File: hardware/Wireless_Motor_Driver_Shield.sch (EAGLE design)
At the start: 84 parts, among them Q1 MOSFET-NCHANNELBSS138, Q2 MOSFET-NCHANNELBSS138, U1 XBEE-1XBEE-1_LOCK, U2 ARDUINO, U3 TB6612FNG

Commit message: Updated after self Eng Design Rules Check
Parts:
- D1: value Red -> Yellow; device SparkFun-LED:LED-RED0603 -> SparkFun-LED:LED-YELLOW0603
- D3: value Yellow -> Red; device SparkFun-LED:LED-YELLOW0603 -> SparkFun-LED:LED-RED0603
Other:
- note added: "B. Huang Revised by Shawn Hymel"
- note added: "Connects Arduino A4 to SDA pin on R3 shield and SDA pin under XBEE radio."
- note removed: "B. Huang Modified by Shawn Hymel"
- moved on the sheet: SJ3, SJ4
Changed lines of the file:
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@@
 <setting verticaltext="up"/>
 </settings>
-<grid distance="0.1" unitdist="inch" unit="inch" style="lines" multiple="1" display="no" altdistance="0.01" altunitdist="inch" altunit="inch"/>
+<grid distance="0.1" unitdist="inch" unit="inch" style="lines" multiple="1" display="yes" altdistance="0.01" altunitdist="inch" altunit="inch"/>
 <layers>
 <layer number="1" name="Top" color="4" fill="1" visible="no" active="no"/>
@@
 <part name="LOGO4" library="SparkFun-Aesthetics" deviceset="SFE_LOGO_NAME_FLAME" device=".1_INCH" value="SFE_LOGO_NAME_FLAME.1_INCH"/>
 <part name="JP22" library="SparkFun-Connectors" deviceset="M04" device="LOCK"/>
-<part name="D1" library="SparkFun-LED" deviceset="LED-RED" device="0603" value="Red"/>
 <part name="D2" library="SparkFun-LED" deviceset="LED-GREEN" device="0603" value="Green"/>
 <part name="R6" library="SparkFun-Resistors" deviceset="1KOHM-1/10W-1%(0603)" device="" value="1K"/>
 <part name="R7" library="SparkFun-Resistors" deviceset="1KOHM-1/10W-1%(0603)" device="" value="1K"/>
-<part name="D3" library="SparkFun-LED" deviceset="LED-YELLOW" device="0603" value="Yellow"/>
 <part name="R8" library="SparkFun-Resistors" deviceset="1KOHM-1/10W-1%(0603)" device="" value="1K"/>
 <part name="GND5" library="SparkFun" deviceset="GND" device=""/>
@@
 <part name="F4" library="SparkFun-PowerIC" deviceset="PTC" device="SMD" value=""/>
 <part name="C3" library="SparkFun-Capacitors" deviceset="10UF" device="-1210-50V-20%" value="10uF"/>
+<part name="D3" library="SparkFun-LED" deviceset="LED-RED" device="0603" value="Red"/>
+<part name="D1" library="SparkFun-LED" deviceset="LED-YELLOW" device="0603" value="Yellow"/>
 </parts>
 <sheets>
@@
 <wire x1="259.08" y1="203.2" x2="259.08" y2="158.75" width="0.2032" layer="97" style="longdash"/>
 <text x="350.52" y="7.62" size="2.54" layer="94">B. Huang
-Modified by Shawn Hymel</text>
+Revised by Shawn Hymel</text>
 <text x="421.64" y="7.62" size="2.54" layer="94">v12</text>
 <wire x1="259.08" y1="158.75" x2="259.08" y2="121.92" width="0.2032" layer="97" style="longdash"/>
@@
 <wire x1="259.08" y1="158.75" x2="431.8" y2="158.75" width="0.1524" layer="97" style="longdash"/>
 <text x="210.82" y="210.82" size="2.54" layer="94">Power Rail Select Switch</text>
-<text x="355.6" y="55.88" size="1.27" layer="97">Max Input Voltage:15V
+<text x="335.28" y="48.26" size="1.778" layer="97">Max Input Voltage:15V
 Output Current: 1.2A (ave) / 3.2A (peak)</text>
-<text x="12.7" y="142.24" size="1.27" layer="97">RESET Jumper provides easy access
+<text x="12.7" y="139.7" size="1.778" layer="97">RESET Jumper provides easy access
 to reset the XBEE Radio Module using
 the flat end of a screwdriver or something
 comparable.</text>
-<text x="76.2" y="203.2" size="1.27" layer="97">Level shifting circuit for XBEE</text>
+<text x="76.2" y="203.2" size="1.778" layer="97">Level shifting circuit for XBEE</text>
 <wire x1="121.92" y1="48.26" x2="177.8" y2="48.26" width="0.2032" layer="97" style="longdash"/>
 <wire x1="177.8" y1="48.26" x2="177.8" y2="5.08" width="0.2032" layer="97" style="longdash"/>
@@
 <wire x1="121.92" y1="5.08" x2="121.92" y2="48.26" width="0.2032" layer="97" style="longdash"/>
 <text x="152.654" y="6.35" size="2.54" layer="94">QC Test Points</text>
-<text x="355.6" y="40.64" size="1.27" layer="97">Dual Motor Driver:
+<text x="386.08" y="38.1" size="1.778" layer="97">Dual Motor Driver:
 Motor A                   Motor B
 ------------------------------------------------
@@
   AIN1 (pin 4)            BIN1 (pin 7)
   AIN2 (pin 5)            BIN2 (pin 8)</text>
+<text x="325.12" y="124.46" size="1.778" layer="97">Connects Arduino A4 to
+SDA pin on R3 shield and
+SDA pin under XBEE radio.</text>
+<text x="373.38" y="124.46" size="1.778" layer="97">Connects Arduino A4 to
+SDA pin on R3 shield and
+SDA pin under XBEE radio.</text>
 </plain>
 <instances>
@@
 <instance part="LOGO4" gate="G$1" x="200.66" y="0"/>
 <instance part="JP22" gate="G$1" x="287.02" y="83.82"/>
-<instance part="D1" gate="G$1" x="12.7" y="43.18"/>
 <instance part="D2" gate="G$1" x="22.86" y="43.18"/>
 <instance part="R6" gate="G$1" x="12.7" y="53.34" rot="R270"/>
 <instance part="R7" gate="G$1" x="22.86" y="53.34" rot="MR270"/>
-<instance part="D3" gate="G$1" x="35.56" y="43.18"/>
 <instance part="R8" gate="G$1" x="35.56" y="53.34" rot="R90"/>
 <instance part="GND5" gate="1" x="35.56" y="33.02"/>
@@
 <instance part="R13" gate="G$1" x="63.5" y="218.44" rot="R90"/>
 <instance part="JP20" gate="G$1" x="284.48" y="139.7"/>
-<instance part="SJ3" gate="G$1" x="342.9" y="142.24" rot="R180"/>
-<instance part="SJ4" gate="G$1" x="398.78" y="142.24" rot="R180"/>
+<instance part="SJ3" gate="G$1" x="332.74" y="144.78" rot="R180"/>
+<instance part="SJ4" gate="G$1" x="381" y="144.78" rot="R180"/>
 <instance part="FRAME1" gate="G$1" x="0" y="0"/>
 <instance part="FRAME1" gate="G$2" x="330.2" y="0"/>
@@
 <instance part="F4" gate="G$1" x="342.9" y="213.36" rot="R180"/>
 <instance part="C3" gate="G$1" x="411.48" y="86.36"/>
+<instance part="D3" gate="G$1" x="35.56" y="43.18"/>
+<instance part="D1" gate="G$1" x="12.7" y="43.18"/>
 </instances>
 <busses>
@@
 <segment>
 <wire x1="35.56" y1="38.1" x2="35.56" y2="35.56" width="0.1524" layer="91"/>
+<pinref part="GND5" gate="1" pin="GND"/>
 <pinref part="D3" gate="G$1" pin="C"/>
-<pinref part="GND5" gate="1" pin="GND"/>
 </segment>
 <segment>
@@
 <segment>
 <pinref part="SJ4" gate="G$1" pin="3"/>
-<wire x1="398.78" y1="147.32" x2="398.78" y2="149.86" width="0.1524" layer="91"/>
-<wire x1="398.78" y1="149.86" x2="406.4" y2="149.86" width="0.1524" layer="91"/>
-<label x="406.4" y="149.86" size="1.27" layer="95" xref="yes"/>
+<wire x1="381" y1="149.86" x2="381" y2="152.4" width="0.1524" layer="91"/>
+<wire x1="381" y1="152.4" x2="388.62" y2="152.4" width="0.1524" layer="91"/>
+<label x="388.62" y="152.4" size="1.27" layer="95" xref="yes"/>
 </segment>
 </net>
@@
 <segment>
 <pinref part="SJ3" gate="G$1" pin="3"/>
-<wire x1="342.9" y1="147.32" x2="342.9" y2="149.86" width="0.1524" layer="91"/>
-<wire x1="342.9" y1="149.86" x2="350.52" y2="149.86" width="0.1524" layer="91"/>
-<label x="350.52" y="149.86" size="1.27" layer="95" xref="yes"/>
+<wire x1="332.74" y1="149.86" x2="332.74" y2="152.4" width="0.1524" layer="91"/>
+<wire x1="332.74" y1="152.4" x2="340.36" y2="152.4" width="0.1524" layer="91"/>
+<label x="340.36" y="152.4" size="1.27" layer="95" xref="yes"/>
 </segment>
 </net>
@@
 <segment>
 <pinref part="SJ3" gate="G$1" pin="1"/>
-<wire x1="342.9" y1="137.16" x2="342.9" y2="134.62" width="0.1524" layer="91"/>
-<wire x1="342.9" y1="134.62" x2="350.52" y2="134.62" width="0.1524" layer="91"/>
-<label x="350.52" y="134.62" size="1.27" layer="95" xref="yes"/>
+<wire x1="332.74" y1="139.7" x2="332.74" y2="137.16" width="0.1524" layer="91"/>
+<wire x1="332.74" y1="137.16" x2="340.36" y2="137.16" width="0.1524" layer="91"/>
+<label x="340.36" y="137.16" size="1.27" layer="95" xref="yes"/>
 </segment>
 </net>
@@
 <segment>
 <pinref part="SJ4" gate="G$1" pin="1"/>
-<wire x1="398.78" y1="137.16" x2="398.78" y2="134.62" width="0.1524" layer="91"/>
-<wire x1="398.78" y1="134.62" x2="406.4" y2="134.62" width="0.1524" layer="91"/>
-<label x="406.4" y="134.62" size="1.27" layer="95" xref="yes"/>
+<wire x1="381" y1="139.7" x2="381" y2="137.16" width="0.1524" layer="91"/>
+<wire x1="381" y1="137.16" x2="388.62" y2="137.16" width="0.1524" layer="91"/>
+<label x="388.62" y="137.16" size="1.27" layer="95" xref="yes"/>
 </segment>
 </net>
@@
 <segment>
 <wire x1="12.7" y1="48.26" x2="12.7" y2="45.72" width="0.1524" layer="91"/>
+<pinref part="R6" gate="G$1" pin="2"/>
 <pinref part="D1" gate="G$1" pin="A"/>
-<pinref part="R6" gate="G$1" pin="2"/>
 </segment>
 </net>
@@
 <segment>
 <wire x1="35.56" y1="48.26" x2="35.56" y2="45.72" width="0.1524" layer="91"/>
+<pinref part="R8" gate="G$1" pin="1"/>
 <pinref part="D3" gate="G$1" pin="A"/>
-<pinref part="R8" gate="G$1" pin="1"/>
 </segment>
 </net>
@@
 <segment>
 <pinref part="SJ4" gate="G$1" pin="2"/>
-<wire x1="403.86" y1="142.24" x2="406.4" y2="142.24" width="0.1524" layer="91"/>
-<label x="406.4" y="142.24" size="1.27" layer="95" xref="yes"/>
+<wire x1="386.08" y1="144.78" x2="388.62" y2="144.78" width="0.1524" layer="91"/>
+<label x="388.62" y="144.78" size="1.27" layer="95" xref="yes"/>
 </segment>
 <segment>
@@
 <segment>
 <pinref part="SJ3" gate="G$1" pin="2"/>
-<wire x1="347.98" y1="142.24" x2="350.52" y2="142.24" width="0.1524" layer="91"/>
-<label x="350.52" y="142.24" size="1.27" layer="95" xref="yes"/>
-</segment>
-<segment>
+<wire x1="337.82" y1="144.78" x2="340.36" y2="144.78" width="0.1524" layer="91"/>
+<label x="340.36" y="144.78" size="1.27" layer="95" xref="yes"/>
+</segment>
+<segment>

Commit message: Added new monster voltage select circuit to servo power rail
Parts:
- removed F1: PTCSMD, SparkFun-PowerIC:PTCSMD
- removed SJ3, SJ4: (no value), SparkFun-Passives:JUMPER-PAD-3-NC_BY_TRACE
- added Q3: MMBT2222A, SparkFun-DiscreteSemi:TRANSISTOR_NPNMMBT2222A
- added Q4: DMG2307L, SparkFun-DiscreteSemi:MOSFET-PCHANNELDMG2307L
- added R14: 1K, SparkFun-Resistors:1KOHM-1/10W-1%(0603)
- added R15, R16: 10K, SparkFun-Resistors:10KOHM-1/10W-1%(0603)0603
- D2: value Green -> GREEN
- D3: value Red -> RED
- D8: value Blue -> GREEN; device SparkFun-LED:LED-BLUE0603 -> SparkFun-LED:LED-GREEN0603
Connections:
- removed net FUSED_VIN: C1.1, C3.1, F1.2, S1.1, S1.4, U3.VM1, U3.VM2, U3.VM3
- removed net SCL_I2C_PORT: JP20.4, SJ4.2
- removed net SDA_I2C_PORT: JP20.3, SJ3.2
- new net N$11: Q3.C, Q4.G, R16.1
- new net N$13: R14.1, S1.1, S1.4
- new net N$2: Q3.B, R14.2, R15.2
- net A4: no longer SJ3.3
- net A5: no longer SJ4.3
- net FUSED_IOREF: now also S1.2, S1.5; no longer S1.3, S1.6
- net GND: now also Q3.E, R15.1
- net PWR_RAIL: now also Q4.D, S1.3, S1.6; no longer S1.2, S1.5
- net SCL: now also JP20.4; no longer SJ4.1
- net SDA: now also JP20.3; no longer SJ3.1
- net VIN: now also C1.1, C3.1, Q4.S, R16.2, U3.VM1, U3.VM2, U3.VM3; no longer F1.1
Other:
- note removed: "Connects Arduino A4 to SDA pin on R3 shield and SDA pin under XBEE radio."
- moved on the sheet: JP20, S1

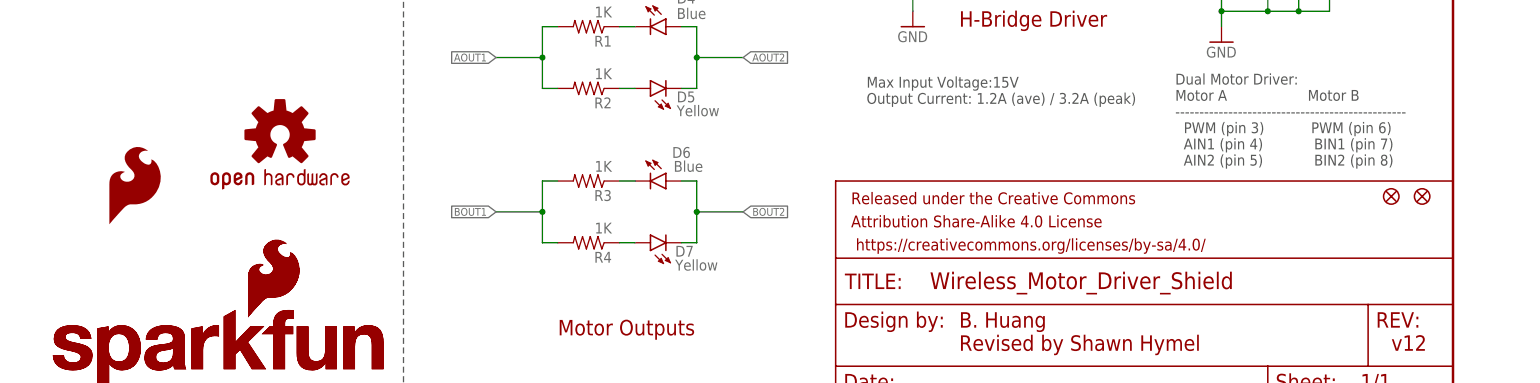
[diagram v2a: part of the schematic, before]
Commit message: Added fiducials, cleaned up silk, added staking vias
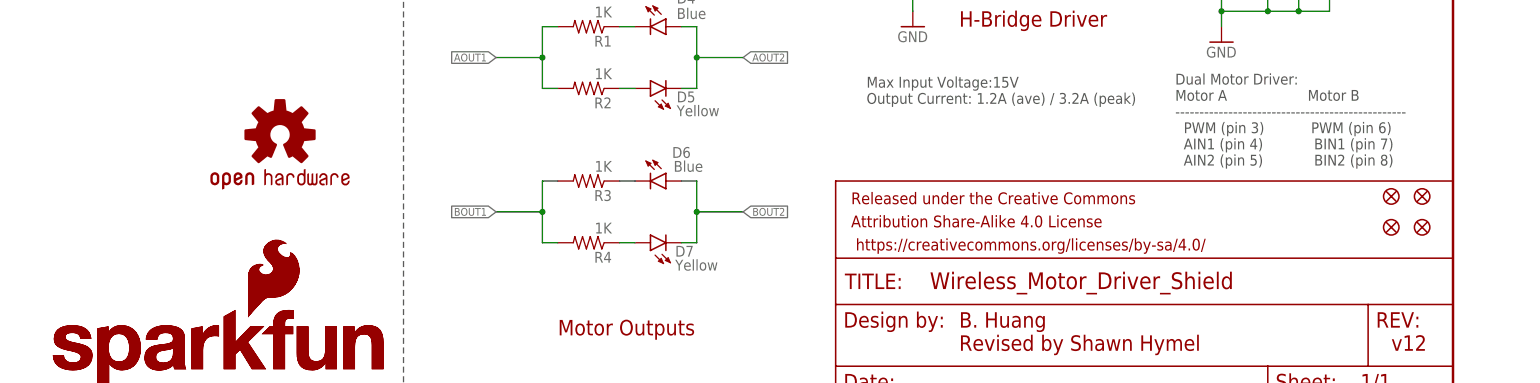
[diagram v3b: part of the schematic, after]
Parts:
- removed LOGO5: SFE_LOGO_FLAME.2COP, SparkFun-Aesthetics:SFE_LOGO_FLAME.2COP
- added FID3, FID4: FIDUCIAL1X2, SparkFun-Aesthetics:FIDUCIAL1X2
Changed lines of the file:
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@@
 <part name="GND9" library="SparkFun-Aesthetics" deviceset="GND" device=""/>
 <part name="GND10" library="SparkFun-Aesthetics" deviceset="GND" device=""/>
-<part name="LOGO5" library="SparkFun-Aesthetics" deviceset="SFE_LOGO_FLAME" device=".2COP" value="SFE_LOGO_FLAME.2COP"/>
 <part name="TP1" library="SparkFun-Passives" deviceset="TEST-POINT" device="3X5" value=""/>
 <part name="TP2" library="SparkFun-Passives" deviceset="TEST-POINT" device="3X5" value=""/>
@@
 <part name="GND11" library="SparkFun-Aesthetics" deviceset="GND" device=""/>
 <part name="GND16" library="SparkFun-Aesthetics" deviceset="GND" device=""/>
+<part name="FID3" library="SparkFun-Aesthetics" deviceset="FIDUCIAL" device="1X2" value="FIDUCIAL1X2"/>
+<part name="FID4" library="SparkFun-Aesthetics" deviceset="FIDUCIAL" device="1X2" value="FIDUCIAL1X2"/>
 </parts>
 <sheets>
@@
 <instance part="GND9" gate="1" x="81.28" y="152.4"/>
 <instance part="GND10" gate="1" x="81.28" y="177.8"/>
-<instance part="LOGO5" gate="G$1" x="210.312" y="27.94"/>
 <instance part="TP1" gate="G$1" x="139.7" y="40.64" smashed="yes">
 <attribute name="NAME" x="137.16" y="40.64" size="1.778" layer="95"/>
@@
 <instance part="GND11" gate="1" x="187.96" y="228.6"/>
 <instance part="GND16" gate="1" x="195.58" y="228.6"/>
+<instance part="FID3" gate="G$1" x="421.64" y="27.94"/>
+<instance part="FID4" gate="G$1" x="426.72" y="27.94"/>
 </instances>
 <busses>

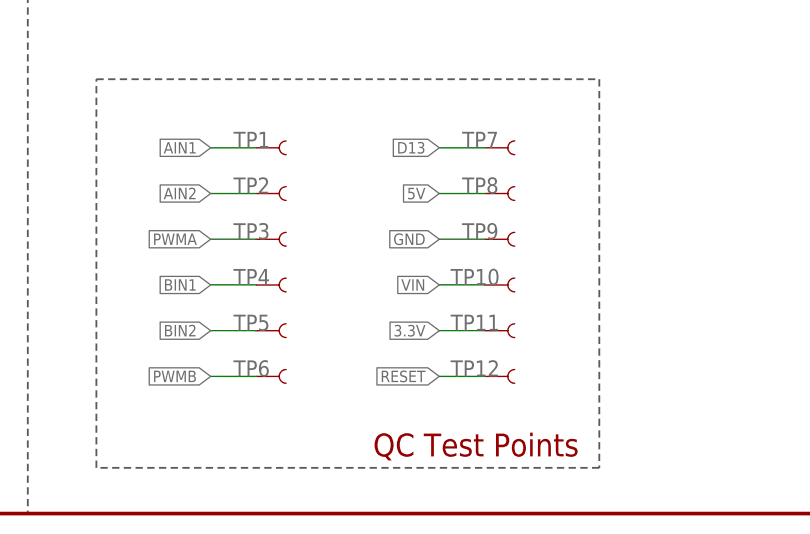
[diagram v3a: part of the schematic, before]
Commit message: Added GND symbol for test point
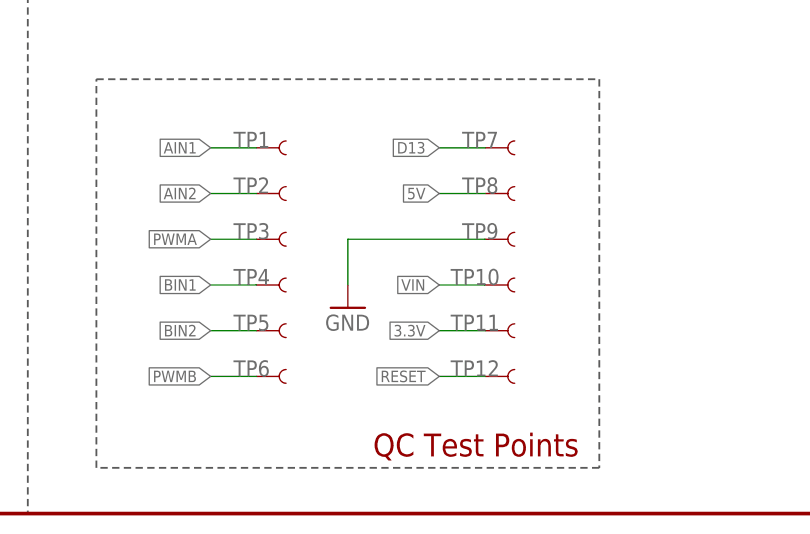
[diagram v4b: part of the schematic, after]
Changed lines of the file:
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@@
 <part name="FID3" library="SparkFun-Aesthetics" deviceset="FIDUCIAL" device="1X2" value="FIDUCIAL1X2"/>
 <part name="FID4" library="SparkFun-Aesthetics" deviceset="FIDUCIAL" device="1X2" value="FIDUCIAL1X2"/>
+<part name="GND17" library="SparkFun" deviceset="GND" device=""/>
 </parts>
 <sheets>
@@
 <instance part="FID3" gate="G$1" x="421.64" y="27.94"/>
 <instance part="FID4" gate="G$1" x="426.72" y="27.94"/>
+<instance part="GND17" gate="1" x="149.86" y="22.86"/>
 </instances>
 <busses>
@@
 <segment>
 <pinref part="TP9" gate="G$1" pin="1"/>
-<wire x1="165.1" y1="30.48" x2="160.02" y2="30.48" width="0.1524" layer="91"/>
-<label x="160.02" y="30.48" size="1.27" layer="95" rot="R180" xref="yes"/>
-</segment>
-<segment>
+<pinref part="GND17" gate="1" pin="GND"/>
+<wire x1="165.1" y1="30.48" x2="149.86" y2="30.48" width="0.1524" layer="91"/>
+<wire x1="149.86" y1="30.48" x2="149.86" y2="25.4" width="0.1524" layer="91"/>
+</segment>
+<segment>

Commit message: Added female I2C header. Added manual selector switch for VIN/VS with new barrel jack to power motors separately.
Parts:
- removed JP20: (no value), SparkFun-Connectors:CONN_04SMD
- added C4: 10uF, SparkFun-Capacitors:10UF-1210-50V-20%
- added D10, D9: B340A, SparkFun-DiscreteSemi:DIODE-SCHOTTKY-B340A
- added J1: 5.5x2.1mm Barrel, SparkFun-Connectors:POWER_JACKSMD
- added J2: (no value), SparkFun-Connectors:M04SMD_RA_FEMALE
- added Q5, Q6: DMG2307L, SparkFun-DiscreteSemi:MOSFET-PCHANNELDMG2307L
- added R17, R18: 10K, SparkFun-Resistors:10KOHM-1/10W-1%(0603)0603
- added S3: (no value), SparkFun-Electromechanical:SWITCH-DPDTAYZ0202
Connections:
- new net N$10: J1.PWR, Q5.S, R17.2
- new net N$12: Q5.G, R17.1, S3.1, S3.4
- new net N$15: D9.A, Q5.D
- new net N$16: D10.A, Q6.D
- new net N$4: Q6.G, R18.1, S3.3, S3.6
- new net VMOTOR: C1.1, C3.1, C4.1, D10.C, D9.C, Q4.S, R16.2, U3.VM1, U3.VM2, U3.VM3
- net FUSED_3.3V: now also J2.2; no longer JP20.2
- net GND: now also C4.2, J1.GNDBREAK, J2.1, S3.2, S3.5; no longer JP20.1
- net SCL: now also J2.4; no longer JP20.4
- net SDA: now also J2.3; no longer JP20.3
- net VIN: now also Q6.S, R18.2; no longer C1.1, C3.1, Q4.S, R16.2, U3.VM1, U3.VM2, U3.VM3
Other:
- note added: "Power Input Select Switch"
- note added: "VS Max Input Voltage:15V"
- note added: "v13"
- note removed: "v12"
- moved on the sheet: D8, F2, F3, F4, R5, S4, U2
